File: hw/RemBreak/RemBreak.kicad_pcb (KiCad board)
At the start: 2 copper layers, 40 x 80 mm, 79 parts, among them IC1 LTC2943IDD#TRPBF, J1 Screw_Terminal_01x04, J2 Screw_Terminal_01x04, J3 Screw_Terminal_01x02, J4 Conn_01x03_MountingPin, J5 Conn_02x06_Odd_Even, J6 Conn_01x07, J7 Conn_01x07, J8 Conn_01x03, Q1 BC337, Q10 BC337, Q11 BC847, Q2 BC847, Q3 BC847, Q4 BC337, Q5 BC337, Q6 SiS415DNT, Q7 BC847, Q8 BC337, Q9 BC847, U1 INA219BxDCN, U2 MAX40200AUK, U3 BD48ExxG, U4 BD48ExxG, U5 L7805, U6 L7805, U7 XC6220B331MR, U8 MAX40200AUK

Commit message: adjusting layout
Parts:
- moved R43 31.5 mm to (153.8, 103.1), turned to 0 degrees
- moved R10 24.0 mm to (148.8, 107.5)
- moved R3 19.8 mm to (141.1, 111.8), turned to 180 degrees
- moved R4 16.8 mm to (141.1, 113.9), turned to 180 degrees
- moved R40 10.1 mm to (125.1, 114.0)
- moved R15 9.98 mm to (146.3, 103.1)
- moved R11 8.26 mm to (141.1, 116.1), turned to 180 degrees
- moved R39 6.02 mm to (125.1, 116.3), turned to 0 degrees
- moved C4 4.96 mm to (146.2, 111.5)
- moved C3 4.72 mm to (130.5, 97.4)
- moved U7 1.67 mm to (146.9, 114.8), turned to 90 degrees
- moved R34 1.52 mm to (149.7, 114.8)
- moved U8 0.99 mm to (146.2, 108.2)
- moved R30 0.38 mm to (146.3, 101.2)
- moved R29 0.25 mm to (146.3, 99.3)
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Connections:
- J6 pad 1: /break_control/BALARM -> /break_control/RF SWITCH
- J6 pad 2: /break_control/RF SWITCH -> /break_control/BALARM
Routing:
- net +3V3: track 114.9 -> 92.6 mm
- net /break_control/BUZZ: track 21.5 -> 13.5 mm
- net +5V: track 77.7 -> 85.0 mm
- net GND: track 11.8 -> 19.0 mm
- net /break_control/BALARM: track 56.3 -> 50.3 mm
- net /break_control/I2C.SCL: track 108.8 -> 102.9 mm
- net /control_connector/ONOFF: track 31.1 -> 35.6 mm, vias 1 -> 2
- net /break_control/VBUS: track 62.3 -> 66.2 mm
- net Net-(U7-VOUT): track 7.58 -> 4.67 mm
- net /break_control/I2C.SDA: track 120.1 -> 117.9 mm
- net /control_connector/LED BLUE: track 36.8 -> 35.0 mm
- net /break_control/RF SWITCH: track 4.60 -> 5.92 mm
- net /control_connector/LED GREEN: track 93.5 -> 94.6 mm
- net /control_connector/LED RED: track 40.8 -> 40.0 mm

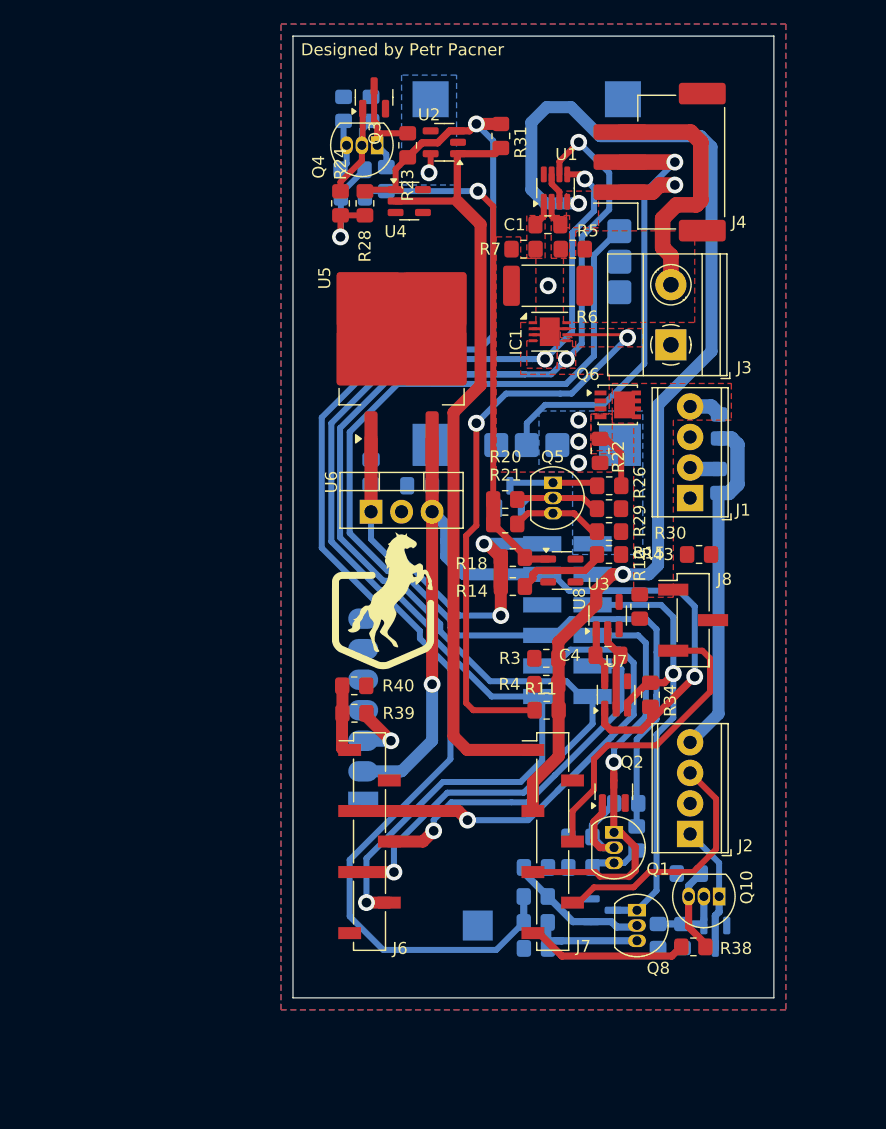
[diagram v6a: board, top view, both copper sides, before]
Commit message: middle part rerouted to fix the gnd connection
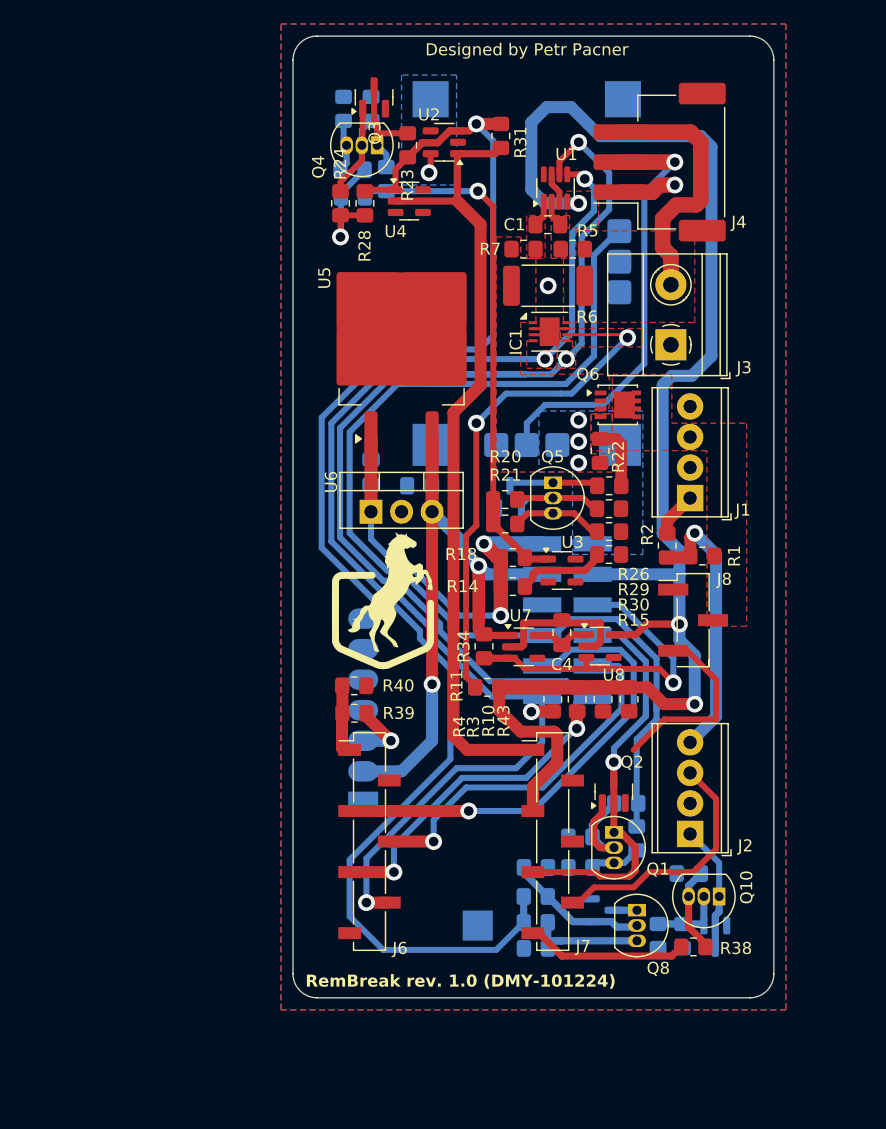
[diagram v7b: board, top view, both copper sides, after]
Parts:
- R1, R2: moved to F.Cu
- moved R34 14.4 mm to (135.9, 110.8), turned to 90 degrees
- moved R43 13.4 mm to (148.0, 115.2), turned to -90 degrees
- moved R1 10.9 mm to (154.1, 103.3), turned to 180 degrees
- moved U7 8.67 mm to (139.2, 110.8), turned to 0 degrees
- moved R10 8.30 mm to (145.8, 115.2)
- moved R2 6.86 mm to (151.1, 102.4)
- moved R11 5.29 mm to (136.2, 114.2)
- moved R3 4.27 mm to (143.6, 115.2), turned to -90 degrees
- moved C4 4.27 mm to (142.4, 109.6), turned to 90 degrees
- moved U8 2.62 mm to (145.5, 110.7), turned to 0 degrees
- moved R4 1.36 mm to (141.6, 115.2), turned to -90 degrees
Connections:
- J1 pad 1: GND -> Net-(J1-Pin_1)
- J1 pad 2: Net-(J1-Pin_2) -> GND
- J1 pad 3: GND -> +7.5V
- J1 pad 4: +7.5V -> GND
- J8 pad 1: +7.5V -> GND
- J8 pad 2: GND -> +7.5V
- R2 pad 1: Net-(J1-Pin_2) -> Net-(J1-Pin_1)
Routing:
- net +3V3: track 92.6 -> 121.7 mm, vias 2 -> 3
- net +5V: track 85.0 -> 58.4 mm
- net /break_control/SERVO: track 25.7 -> 15.8 mm
- net /control_connector/LED RED: track 40.0 -> 30.2 mm
- net /break_control/DISPLAY.DI: track 46.9 -> 39.7 mm
- net /break_control/BALARM: track 50.3 -> 43.4 mm
- net Net-(J2-Pin_4): track 28.6 -> 23.1 mm, vias 0 -> 1
- net GND: track 19.0 -> 24.3 mm
- net Net-(J1-Pin_1): track 0.00 -> 3.74 mm
- net +7.5V: track 2.69 -> 0.00 mm
- net Net-(J1-Pin_2): track 2.42 -> 0.00 mm
- net /break_control/I2C.SDA: track 117.9 -> 120.2 mm, vias 3 -> 4
- net /control_connector/LED GREEN: track 94.6 -> 93.2 mm
- net /control_connector/LED BLUE: track 35.0 -> 34.1 mm
- net /break_control/I2C.SCL: track 102.9 -> 103.8 mm, vias 3 -> 4
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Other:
- outline, holes or cut-outs redrawn
- board text added: "RemBreak rev. 1.0 (DMY-101224)"

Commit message: finished routing - drc did not pass
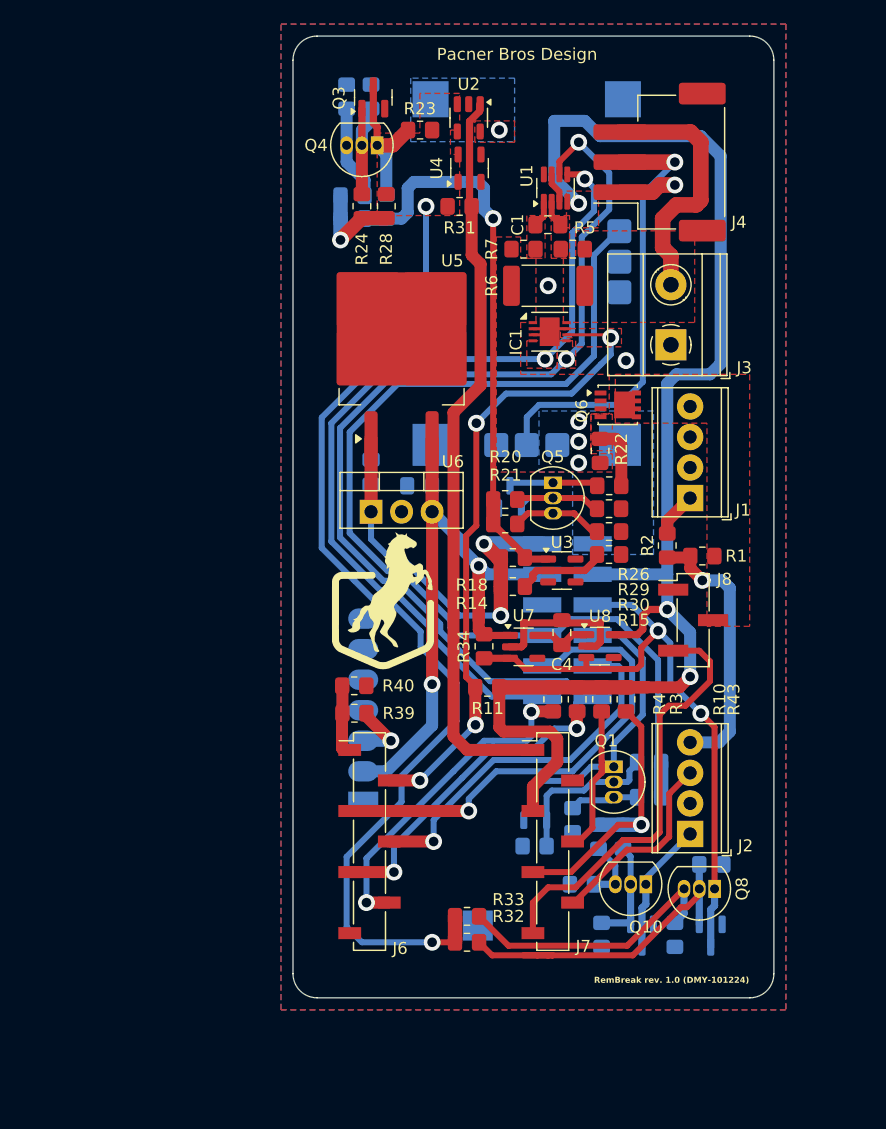
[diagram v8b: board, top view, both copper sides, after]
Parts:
- Q2, R38: moved to B.Cu
- R32, R33: moved to F.Cu
- moved R35 14.6 mm to (154.8, 128.9)
- moved R38 12.1 mm to (145.4, 126.6), turned to -90 degrees
- moved R36 11.6 mm to (151.8, 134.8), turned to 90 degrees
- moved R37 9.63 mm to (147.4, 126.6), turned to -90 degrees
- moved Q9 9.27 mm to (154.7, 134.8), turned to -90 degrees
- moved R42 8.93 mm to (144.0, 130.6)
- moved R32 6.87 mm to (134.5, 135.4)
- moved R31 6.79 mm to (133.9, 74.2), turned to 0 degrees
- moved Q8 6.70 mm to (155.1, 130.9), turned to 180 degrees
- moved Q2 6.69 mm to (140.1, 124.3)
- moved Q10 6.18 mm to (149.4, 130.6)
- moved Q11 6.10 mm to (149.0, 134.8)
- moved R33 5.74 mm to (134.5, 133.2)
- moved U4 5.71 mm to (134.7, 71.0), turned to 90 degrees
- moved Q1 5.46 mm to (146.7, 120.8)
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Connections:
- J1 pad 3: +7.5V -> GND
- J1 pad 4: GND -> +7.5V
- J7 pad 4: /break_control/SERVO -> /control_connector/LED BLUE
- J7 pad 5: /control_connector/LED BLUE -> /break_control/BUZZ
- J7 pad 7: /break_control/BUZZ -> /break_control/SERVO
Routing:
- net /power_manager/EN: track 123.4 -> 85.0 mm, vias 1 -> 2
- net /control_connector/LED RED: track 30.2 -> 55.7 mm, vias 1 -> 2
- net /break_control/SERVO: track 15.8 -> 35.7 mm
- net Net-(Q8-B): track 11.8 -> 28.8 mm
- net Net-(Q8-E): track 10.2 -> 23.2 mm
- net /break_control/BUZZ: track 13.5 -> 24.2 mm, vias 0 -> 1
- net /break_control/BALARM: track 43.4 -> 53.6 mm, vias 2 -> 4
- net /break_control/I2C.SDA: track 120.2 -> 112.3 mm
- net /control_connector/LED GREEN: track 93.2 -> 85.7 mm
- net +3V3: track 121.7 -> 116.0 mm
- net /break_control/VBUS: track 66.2 -> 61.3 mm
- net /break_control/I2C.SCL: track 103.8 -> 99.0 mm
- net /break_control/BUTTON: track 21.0 -> 16.4 mm
- net Net-(Q4-E): track 4.38 -> 7.86 mm
- net /control_connector/LED BLUE: track 34.1 -> 37.6 mm, vias 1 -> 0
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- added copper zone on F.Cu, net /power_manager/EN
- added copper zone on F.Cu, net Net-(M1-Vin)
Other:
- board text added: "Pacner Bros Design"
- board text removed: "Designed by Petr Pacner"
